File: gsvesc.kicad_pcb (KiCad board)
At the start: 4 copper layers, 111 x 111 mm, 138 parts, among them J1 Conn_01x06, J10 PHASE_C, J11 PHASE_B, J12 NTC, J13 Conn_01x02, J14 Conn_02x04_Odd_Even, J2 Conn_01x06, J3 Conn_01x06, J4 Conn_01x05, J5 Conn_01x03, J6 USB_B_Mini, J7 BAT+, J8 BAT-, J9 PHASE_A, Q1 TPH2R506PL, Q2 TPH2R506PL, Q3 TPH2R506PL, Q4 TPH2R506PL, Q5 TPH2R506PL, Q6 TPH2R506PL, U1 STM32F405RGTx, U10 LM5008MM, U11 M74VHC1GT66DTT1G, U12 LM5107, U13 M74VHC1GT66DTT1G, U14 TPS5430DDA, U15 LM5107, U2 M74VHC1GT66DTT1G, U3 LM5107, U4 INA240A3, U5 INA240A3, U6 INA240A3, U7 M74VHC1GT66DTT1G, U8 M74VHC1GT66DTT1G, U9 M74VHC1GT66DTT1G, Y1 ABM3B 8MHz

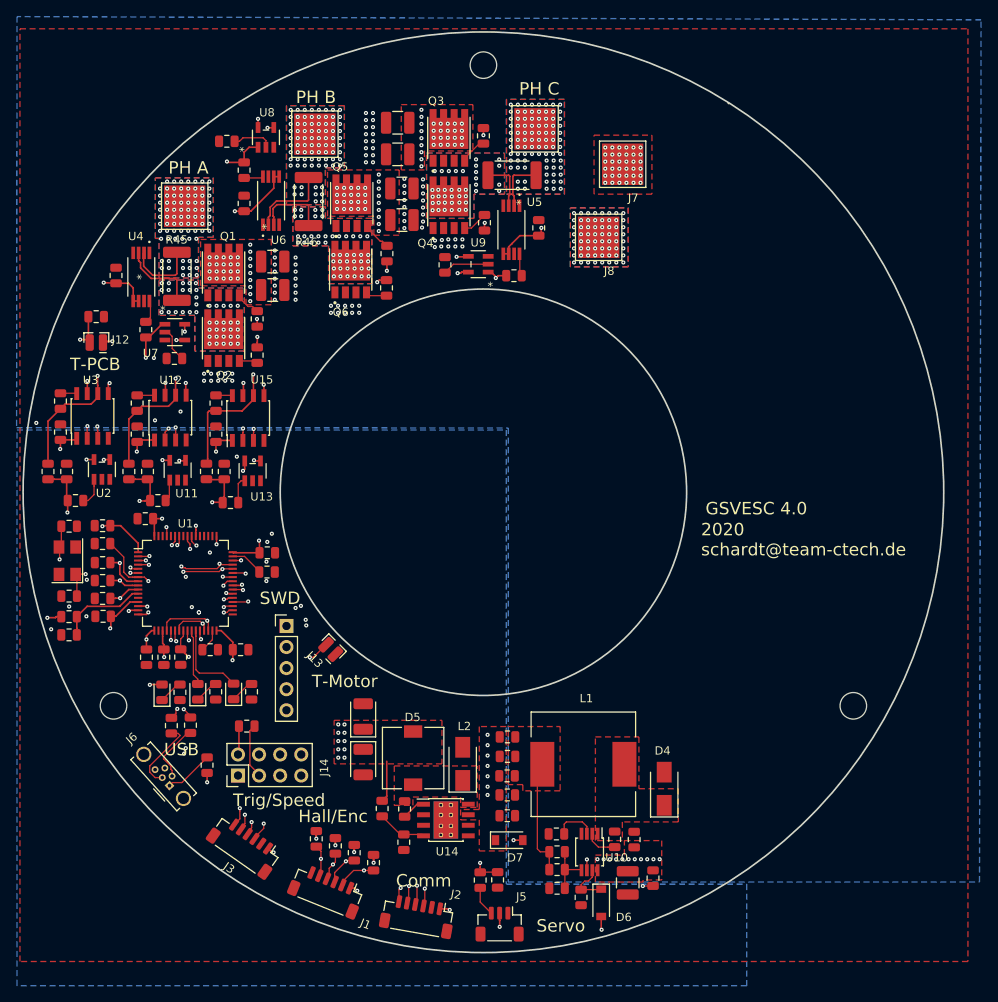
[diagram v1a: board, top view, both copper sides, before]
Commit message: Add boot-diode to use LM5109A as alternative FET driver
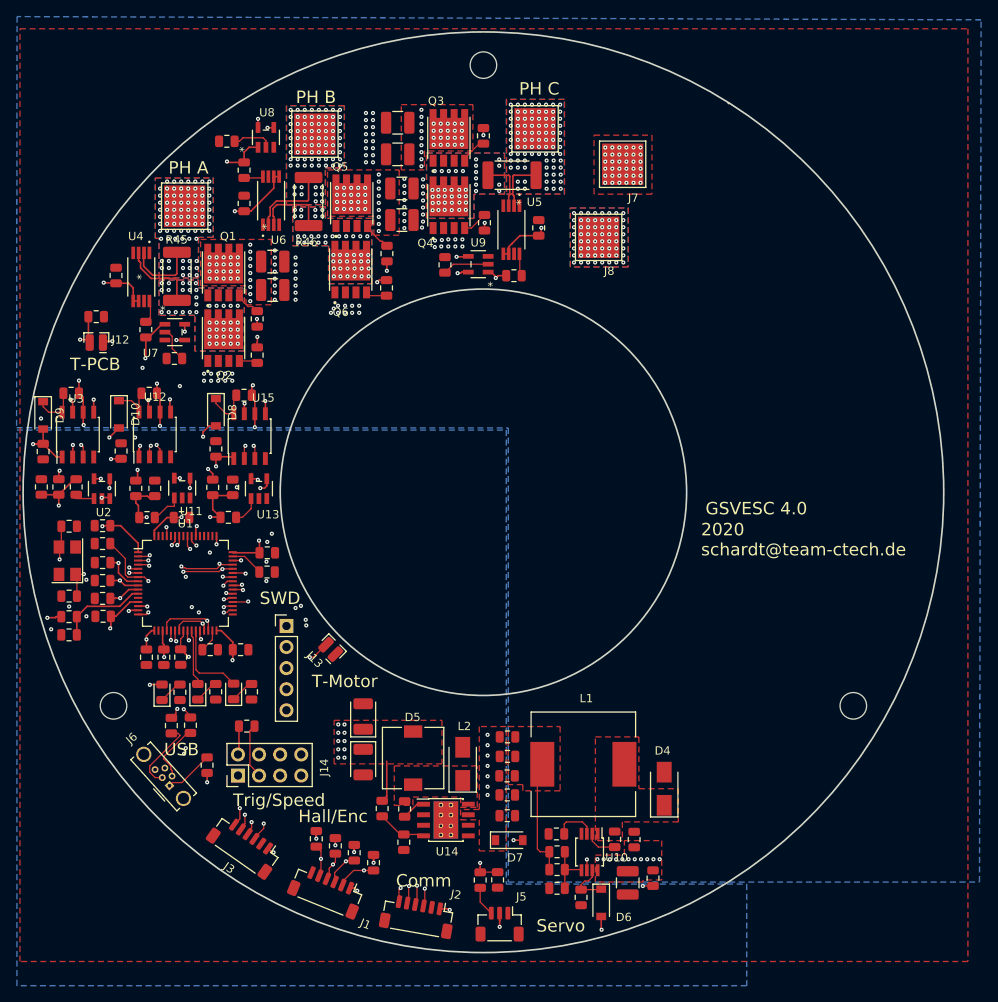
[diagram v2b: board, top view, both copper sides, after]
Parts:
- added D10: B5819W, Diode_SMD:D_SOD-123, F.Cu at (56.1, 90.6)
- added D8: B5819W, Diode_SMD:D_SOD-123, F.Cu at (67.7, 90.3)
- added D9: B5819W, Diode_SMD:D_SOD-123, F.Cu at (46.9, 90.7)
- Q1, Q2, Q3, Q4, Q5, Q6: value TPH2R506PL -> TPH2R608NH,L1Q
- R31, R45, R46: value 0R0005 -> 0R001
- R36, R41: value 10K0 -> 10k0
- U11, U13, U2, U7, U8, U9: value M74VHC1GT66DTT1G -> SN74LVC1G66DBVR
- U4, U5, U6: value INA240A3 -> INA240A2
- moved C12 4.37 mm to (63.6, 103.0), turned to 180 degrees
- moved R14 3.57 mm to (46.7, 99.4)
- moved C32 3.52 mm to (71.1, 88.3), turned to 0 degrees
- moved C15 3.14 mm to (46.9, 95.1), turned to 270 degrees
- moved U3 2.86 mm to (51.1, 93.0)
- moved C22 2.81 mm to (56.3, 95.0)
- moved U12 2.76 mm to (60.4, 93.0)
- moved C25 2.43 mm to (59.4, 103.0)
- moved U2 2.32 mm to (54.0, 99.6)
- moved U13 2.28 mm to (72.9, 99.6)
- moved R13 2.27 mm to (48.8, 99.4)
- moved U11 2.21 mm to (63.7, 99.5)
- moved R18 2.21 mm to (60.4, 99.5)
- moved R17 2.20 mm to (58.1, 99.5)
- moved U15 2.19 mm to (71.8, 93.2)
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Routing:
- net +12V: track 11.4 -> 17.9 mm, vias 11 -> 14
- net /POWER/CURR_FILTER: track 109.7 -> 104.8 mm
- net /Driver/GL_A: track 23.4 -> 28.0 mm
- net /Driver/GL_B: track 30.8 -> 35.4 mm
- net Net-(C21-Pad1): track 1.98 -> 5.51 mm
- net Net-(C32-Pad1): track 2.00 -> 5.51 mm
- net Net-(C27-Pad1): track 2.10 -> 5.59 mm
- net /Driver/GH_A: track 26.9 -> 30.2 mm
- net /Driver/GH_B: track 35.0 -> 38.1 mm
- net /Driver/SENS_FILTER: track 38.0 -> 35.5 mm
- net /Driver/SENS_B: track 21.2 -> 18.9 mm
- net /MCU/H3: track 20.9 -> 18.6 mm
- net /MCU/L1: track 42.9 -> 40.8 mm
- net /Driver/GL_C: track 41.0 -> 42.9 mm
- net /MCU/L3: track 24.4 -> 22.5 mm
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
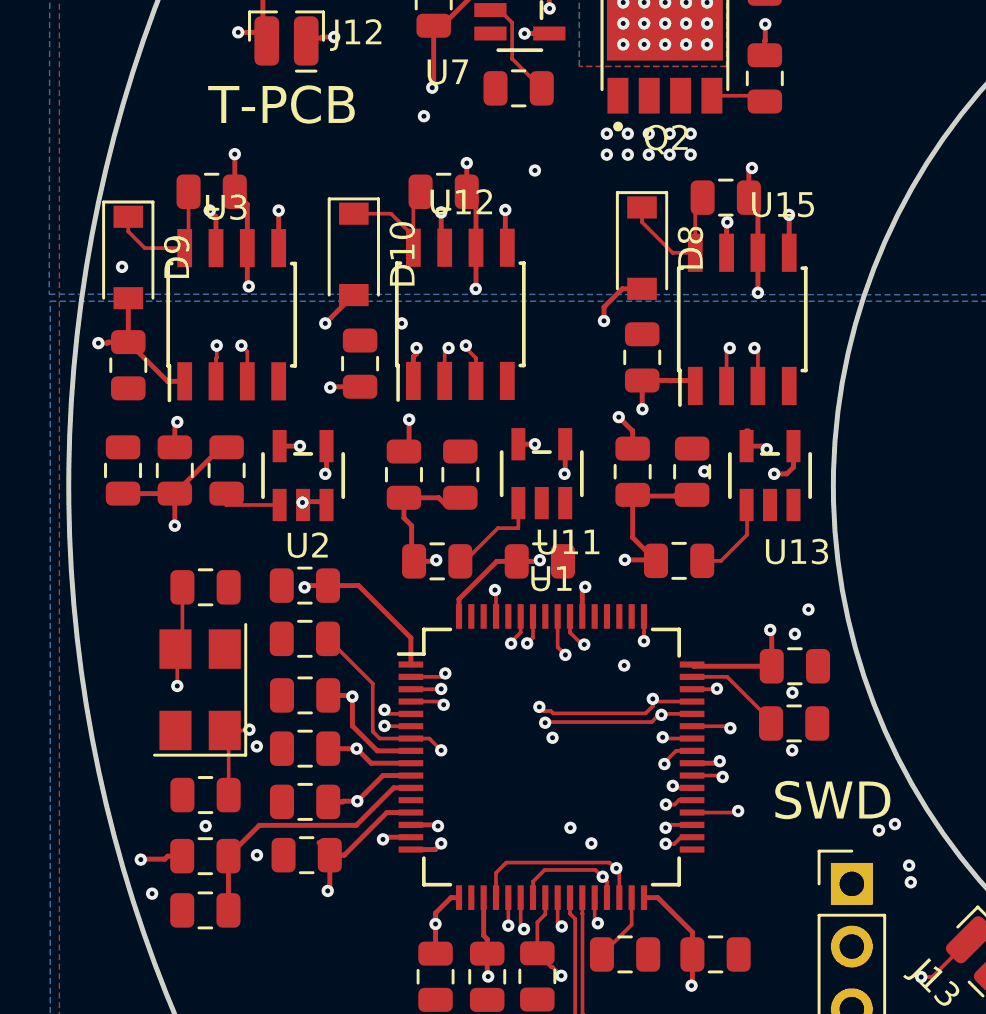
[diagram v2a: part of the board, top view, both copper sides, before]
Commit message: einige Bauteile geändert, so dass sie Basic Parts bei JLC sind
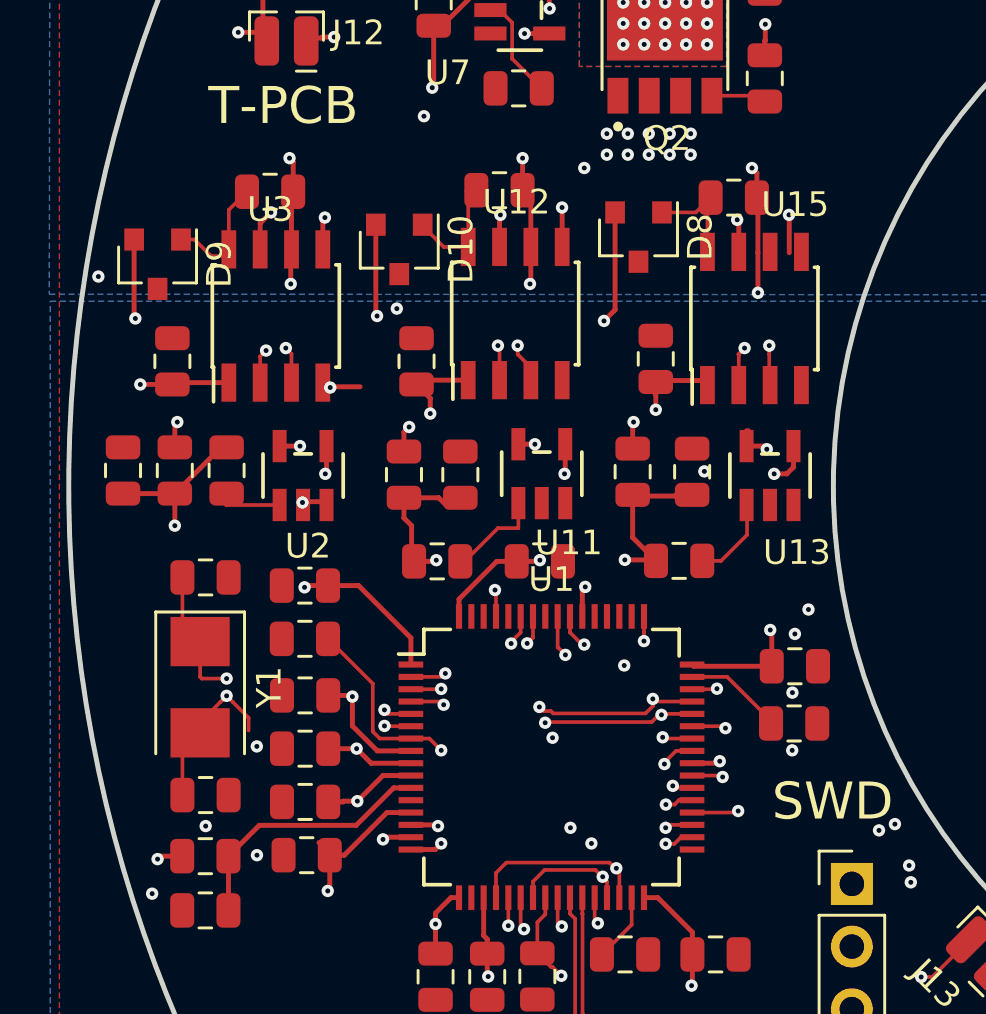
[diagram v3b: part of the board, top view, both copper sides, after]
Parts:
- D10, D8, D9: value B5819W -> SMMBD914LT3G; footprint Diode_SMD:D_SOD-123 -> Package_TO_SOT_SMD:SOT-23
- Y1: value ABM3B 8MHz -> X50328MSB2GI; footprint Crystal:Crystal_SMD_5032-4Pin_5.0x3.2mm -> Crystal:Crystal_SMD_5032-2Pin_5.0x3.2mm
- moved C21 2.37 mm to (52.7, 88.1)
- moved C22 2.29 mm to (58.6, 94.9)
- moved C27 2.26 mm to (62.0, 88.0)
- moved U12 2.22 mm to (62.6, 93.0)
- moved D10 1.85 mm to (57.9, 90.4)
- moved C15 1.79 mm to (48.7, 94.9), turned to 90 degrees
- moved U3 1.79 mm to (52.9, 93.1)
- moved D9 1.22 mm to (48.1, 91.0)
- moved C29 0.55 mm to (68.3, 94.8)
- moved U15 0.50 mm to (72.3, 93.2)
- moved D8 0.47 mm to (67.6, 89.9)
- moved C3 0.40 mm to (50.0, 103.7)
- moved C32 0.33 mm to (71.5, 88.3)
- moved Y1 0.10 mm to (49.8, 108.1), turned to 270 degrees
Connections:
- C4 pad 1: GND -> Net-(C4-Pad1)
- C4 pad 2: Net-(C4-Pad2) -> GND
- U1 pad 6: Net-(C4-Pad2) -> Net-(C4-Pad1)
- Y1 pad 1: Net-(C4-Pad2) -> Net-(C3-Pad1)
- Y1 pad 2: GND -> Net-(C4-Pad1)
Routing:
- net Net-(C4-Pad1): track 0.00 -> 14.5 mm, vias 0 -> 2
- net Net-(C4-Pad2): track 10.3 -> 0.00 mm, vias 2 -> 0
- net +12V: track 17.9 -> 25.4 mm
- net /Driver/GL_B: track 35.4 -> 32.6 mm
- net /Driver/GH_B: track 38.1 -> 35.6 mm
- net /POWER/CURR_FILTER: track 104.8 -> 102.8 mm
- net /Driver/SH_C: track 56.5 -> 54.6 mm
- net /Driver/SH_B: track 48.7 -> 47.4 mm
- net GND: track 1.62 -> 2.84 mm, vias 142 -> 143
- net Net-(C32-Pad1): track 5.51 -> 4.48 mm
- net /Driver/GL_A: track 28.0 -> 27.1 mm
- net /MCU/H1: track 36.7 -> 35.8 mm
- net /Driver/GH_A: track 30.2 -> 29.3 mm
- net /MCU/L2: track 27.9 -> 27.0 mm
- net /MCU/H2: track 24.9 -> 24.2 mm

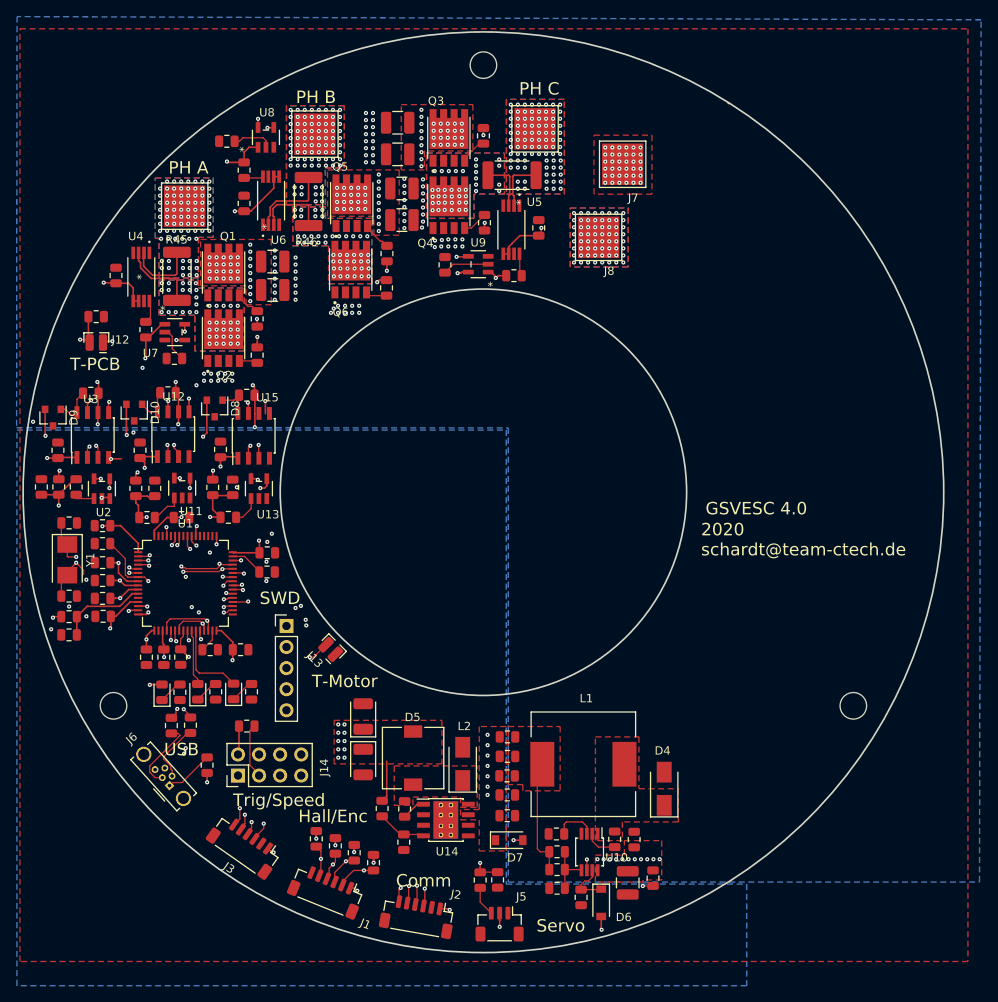
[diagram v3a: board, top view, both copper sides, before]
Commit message: BLE Modul hinzugefügt, optional
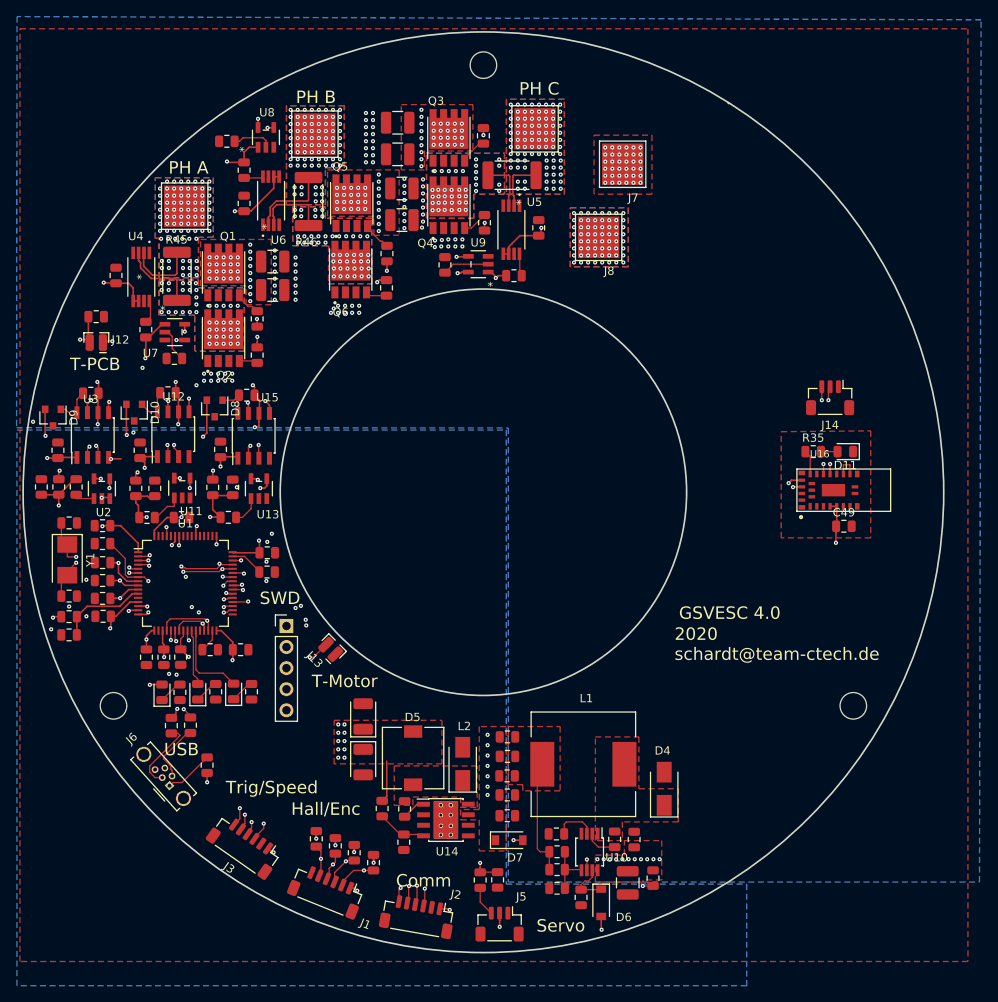
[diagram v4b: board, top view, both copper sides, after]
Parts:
- removed R41: 10k0, Resistor_SMD:R_0805_2012Metric
- added C49: 10u0/25V, Capacitor_SMD:C_0805_2012Metric, F.Cu at (143.5, 104.1)
- added D11: RED, LED_SMD:LED_0805_2012Metric, F.Cu at (143.6, 95.1)
- added R35: 4k70, Resistor_SMD:R_0805_2012Metric, F.Cu at (139.8, 95.1)
- added U16: EYSGJNZWY, gsvesc:BLE_EYSGJNZWY, F.Cu at (137.8, 102.3)
- J14: value Conn_02x04_Odd_Even -> Conn_01x03; footprint Connector_PinHeader_2.54mm:PinHeader_2x04_P2.54mm_Vertical -> Connector_JST:JST_SH_BM03B-SRSS-TB_1x03-1MP_P1.00mm_Vertical
- R27: value 10k0 -> 13k0
- R34: value 5k90 -> 7k50
- moved J14 84.7 mm to (141.8, 88.6), turned to 180 degrees
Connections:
- J14 pad 2: VCC -> Net-(J14-Pad2)
- U1 pad 28: /NRF/GPIO1 -> /MCU/PB2
- U1 pad 55: /NRF/GPIO2 -> /MCU/PB3
- U1 pad 56: /NRF/GPIO3 -> /MCU/PB4
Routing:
- net /NRF/NRF_TX: track 41.2 -> 111.2 mm, vias 2 -> 3
- net /NRF/NRF_RX: track 44.6 -> 111.7 mm, vias 2 -> 3
- net /NRF/GPIO3: track 35.0 -> 0.00 mm, vias 2 -> 0
- net /NRF/GPIO2: track 34.4 -> 0.00 mm, vias 1 -> 0
- net /NRF/GPIO1: track 18.0 -> 0.00 mm, vias 1 -> 0
- net Net-(J14-Pad2): track 0.00 -> 10.7 mm, vias 0 -> 2
- net Net-(J14-Pad3): track 6.73 -> 10.6 mm, vias 0 -> 2
- net Net-(U16-Pad13): track 0.00 -> 3.00 mm
- net Net-(R35-Pad1): track 0.00 -> 2.94 mm
- net Net-(D11-Pad2): track 0.00 -> 2.00 mm
- net VCC: track 76.2 -> 78.0 mm, vias 35 -> 36
- net Net-(C4-Pad1): track 14.5 -> 12.7 mm
- net /MCU/HALL_1: track 43.1 -> 41.7 mm
- net /MCU/HALL_3: track 44.6 -> 43.2 mm
- net /MCU/HALL_2: track 43.9 -> 42.5 mm

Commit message: V4 before review
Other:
- board text added: "BLE Modul"
- board text added: "BLE SWD"
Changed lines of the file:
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@@
   (general
     (thickness 1.6)
-    (drawings 16)
+    (drawings 18)
     (tracks 1792)
     (zones 0)
@@
     (1 In1.Cu signal)
     (2 In2.Cu signal)
-    (31 B.Cu signal hide)
+    (31 B.Cu signal)
     (32 B.Adhes user hide)
     (33 F.Adhes user hide)
@@
       (drillshape 0)
       (scaleselection 1)
-      (outputdirectory "/home/schardt/privat/projekte/scooter/kicad/gsvesc/gerber/"))
+      (outputdirectory "gerber/"))
   )
   (net 0 "")
@@
     (at 137.7998 102.2998)
     (attr smd)
-    (fp_text reference U16 (at 2.7534 -6.90856) (layer F.SilkS)
+    (fp_text reference U16 (at -1.8 -0.4) (layer F.SilkS)
       (effects (font (size 0.867213 0.867213) (thickness 0.015)))
     )
@@
     (tags capacitor)
     (attr smd)
-    (fp_text reference C49 (at 0 -1.65) (layer F.SilkS)
+    (fp_text reference C49 (at 0 -1.65) (layer F.SilkS) hide
       (effects (font (size 1 1) (thickness 0.15)))
     )
@@
     (tags "connector JST SH side entry")
     (attr smd)
-    (fp_text reference J14 (at 0 -3.3 180) (layer F.SilkS)
+    (fp_text reference J14 (at 0 -3.3 180) (layer F.SilkS) hide
       (effects (font (size 1 1) (thickness 0.15)))
     )
@@
     (tags diode)
     (attr smd)
-    (fp_text reference D11 (at 0 -1.65 180) (layer F.SilkS)
+    (fp_text reference D11 (at 0 -1.65 180) (layer F.SilkS) hide
       (effects (font (size 1 1) (thickness 0.15)))
     )
@@
     (tags resistor)
     (attr smd)
-    (fp_text reference R35 (at 0 -1.65) (layer F.SilkS)
+    (fp_text reference R35 (at 0 -1.65) (layer F.SilkS) hide
       (effects (font (size 1 1) (thickness 0.15)))
     )
@@
     )
   )
+  (gr_text "BLE SWD" (at 143.4998 84.4998) (layer F.SilkS)
+    (effects (font (size 1.5 1.5) (thickness 0.15)))
+  )
+  (gr_text "BLE Modul" (at 139.6998 106.6998) (layer F.SilkS)
+    (effects (font (size 1.5 1.5) (thickness 0.15)))
+  )
   (gr_text T-PCB (at 53.1998 84.5798) (layer F.SilkS)

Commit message: small changes
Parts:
- moved R16 2.25 mm to (108.9, 145.6)
- moved C23 2.10 mm to (108.9, 143.4)
- moved D4 0.62 mm to (121.2, 135.9)
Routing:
- net GND: track 2.84 -> 6.57 mm, vias 143 -> 150
- net VCC: track 78.0 -> 80.1 mm
